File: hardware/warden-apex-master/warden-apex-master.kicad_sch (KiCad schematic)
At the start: 82 parts, among them IC1 SIM7080G, IC2 BQ24650RVAR, IC3 TPS63070RNMR, IC4 MAX98357AETE+T, J1 U.FL-R-SMT-1, J2 U.FL-R-SMT-1, J3 61300211121, J4 Expansion_Header, J5 Qwiic, Q1 DMG9926UDM, Q2 AO3401A, Q3 2N7002, U1 113991115, U2 Ai-Thinker-Ra-01, U3 M138 Modem, U4 MCP23017_SO, U5 SRV05-4-P-T7, U6 SC16IS740, X1 14.7456MHz

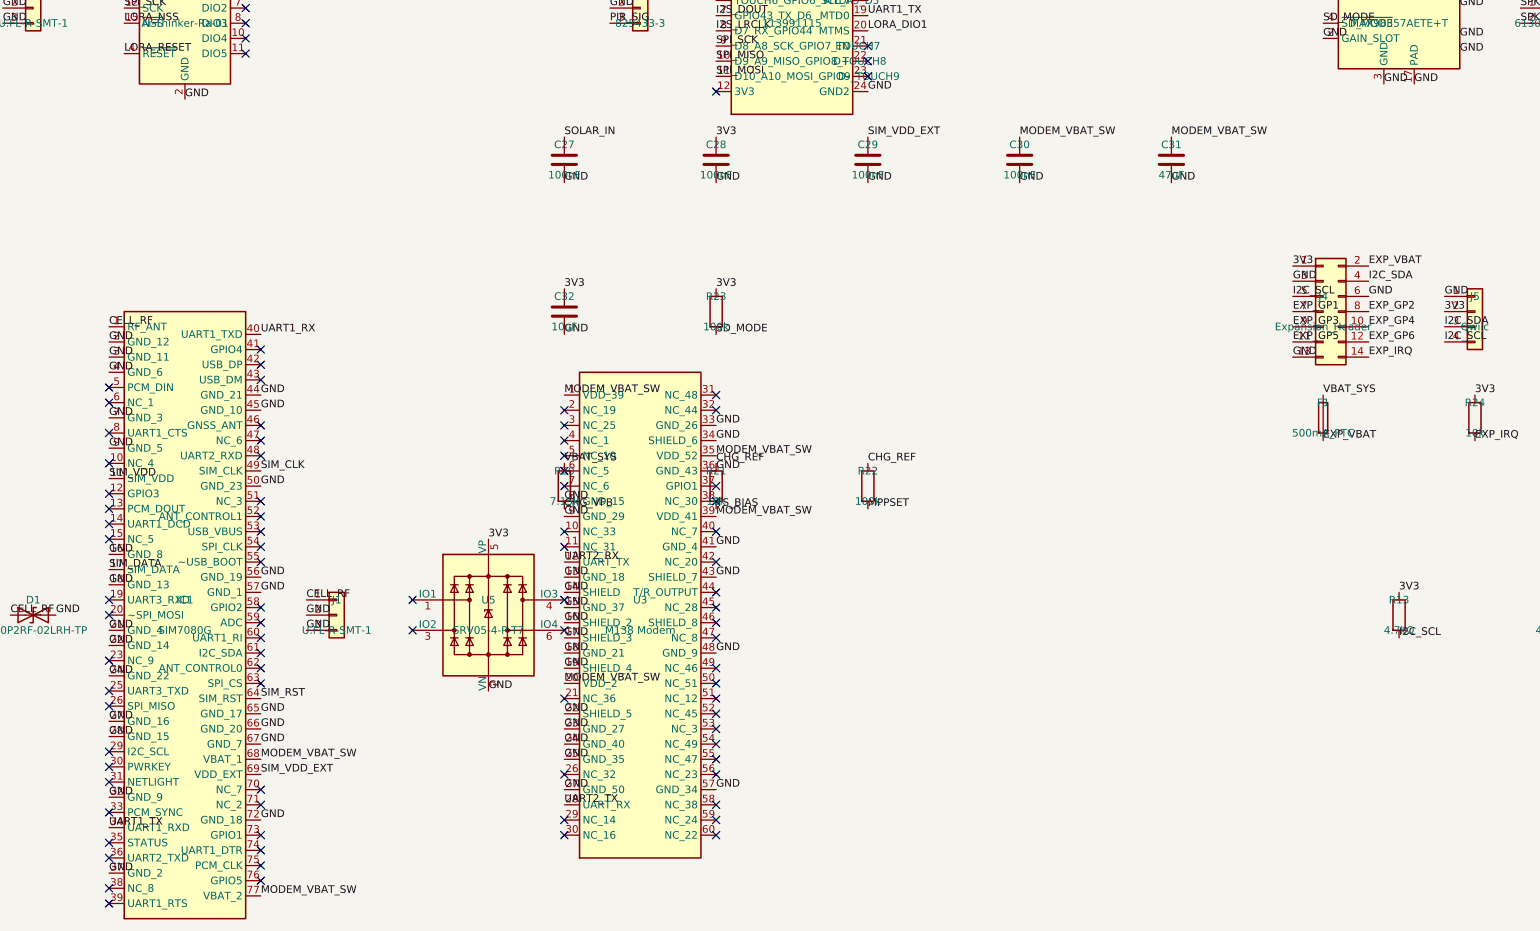
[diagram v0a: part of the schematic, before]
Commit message: Update warden-apex design for Phase 21 SIM7080 repair. Adjusted BOM files to include new capacitor C33 and updated component placements for C34. Revised Gerber files with new timestamps and corrected net connections for UART signals. Enhanced README.md with details on the repair process and updated upload instructions for JLCPCB.
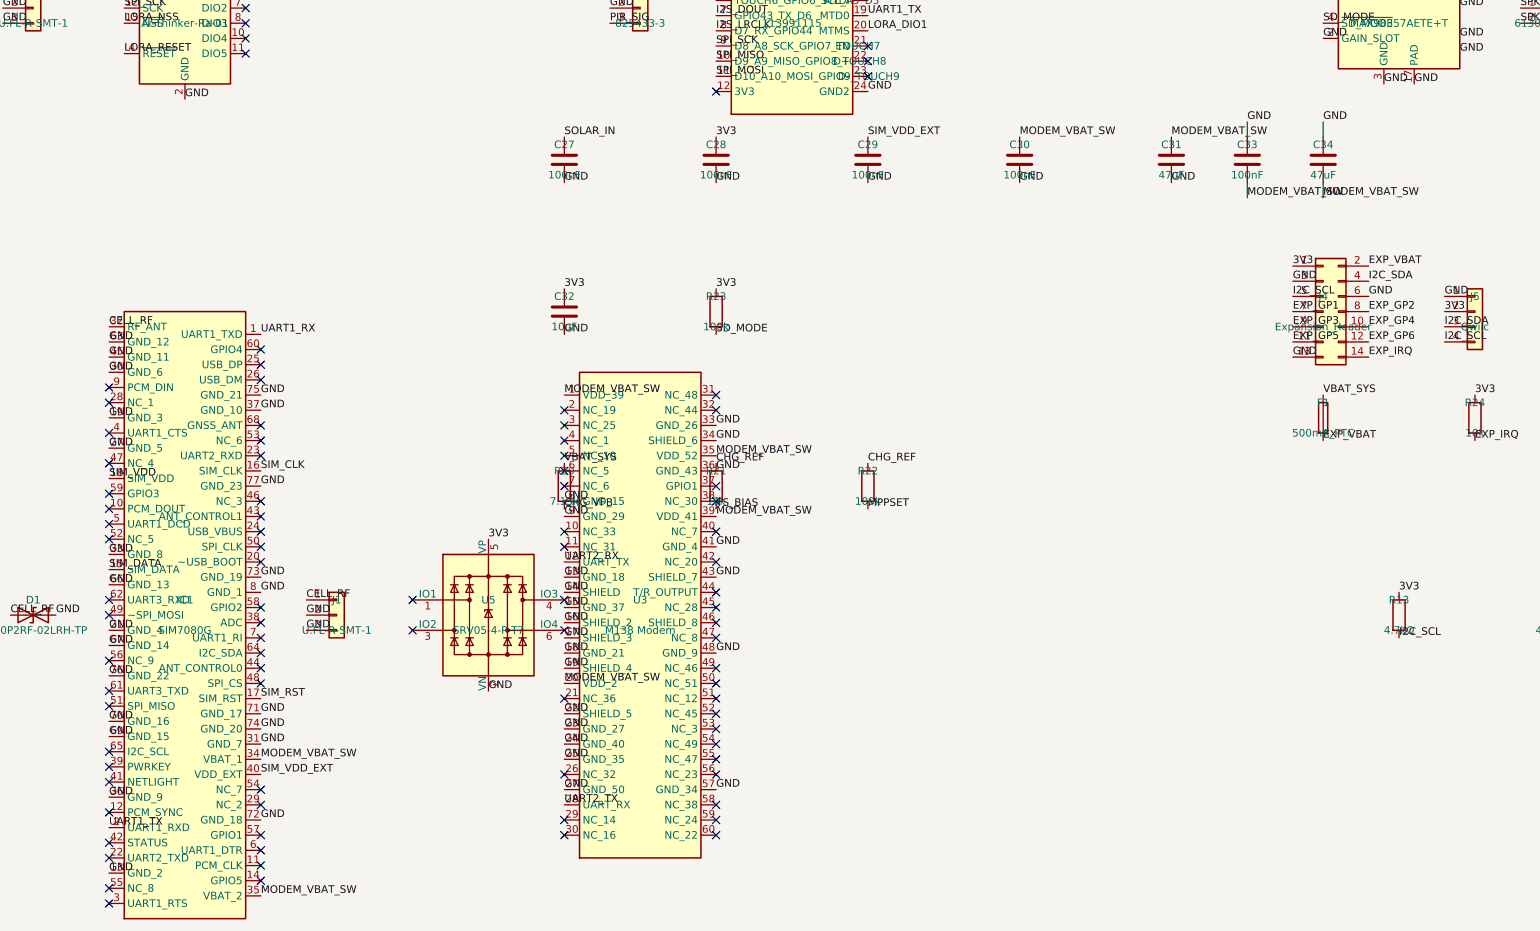
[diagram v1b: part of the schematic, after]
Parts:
- added C33: 100nF, Capacitor_SMD:C_0805_2012Metric, symbol Device:C
- added C34: 47uF, Capacitor_SMD:C_1206_3216Metric, symbol Device:C
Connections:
- net CELL_RF: now also IC1.32 (RF_ANT); no longer IC1.1 (RF_ANT)
- net GND: now also IC1.13 (GND_2), IC1.19 (GND_3), IC1.30 (GND_6), IC1.31 (GND_7), IC1.33 (GND_8), IC1.36 (GND_9), IC1.63 (GND_12), IC1.69 (GND_15), IC1.70 (GND_16), IC1.71 (GND_17), IC1.73 (GND_19), IC1.74 (GND_20), IC1.75 (GND_21), IC1.76 (GND_22), IC1.77 (GND_23), IC1.8 (GND_1), C33.1, C34.1; no longer IC1.16 (GND_8), IC1.18 (GND_13), IC1.2 (GND_12), IC1.22 (GND_14), IC1.24 (GND_22), IC1.28 (GND_15), IC1.3 (GND_11), IC1.32 (GND_9), IC1.4 (GND_6), IC1.44 (GND_21), IC1.50 (GND_23), IC1.56 (GND_19), IC1.57 (GND_1), IC1.65 (GND_17), IC1.7 (GND_3), IC1.9 (GND_5)
- net MODEM_VBAT_SW: now also IC1.34 (VBAT_1), IC1.35 (VBAT_2), C33.2, C34.2; no longer IC1.68 (VBAT_1), IC1.77 (VBAT_2)
- net SIM_CLK: now also IC1.16 (SIM_CLK); no longer IC1.49 (SIM_CLK)
- net SIM_DATA: now also IC1.15 (SIM_DATA); no longer IC1.17 (SIM_DATA)
- net SIM_RST: now also IC1.17 (SIM_RST); no longer IC1.64 (SIM_RST)
- net SIM_VDD: now also IC1.18 (SIM_VDD); no longer IC1.11 (SIM_VDD)
- net SIM_VDD_EXT: now also IC1.40 (VDD_EXT); no longer IC1.69 (VDD_EXT)
- net UART1_RX: now also IC1.1 (UART1_TXD); no longer IC1.40 (UART1_TXD)
- net UART1_TX: now also IC1.2 (UART1_RXD); no longer IC1.34 (UART1_RXD)

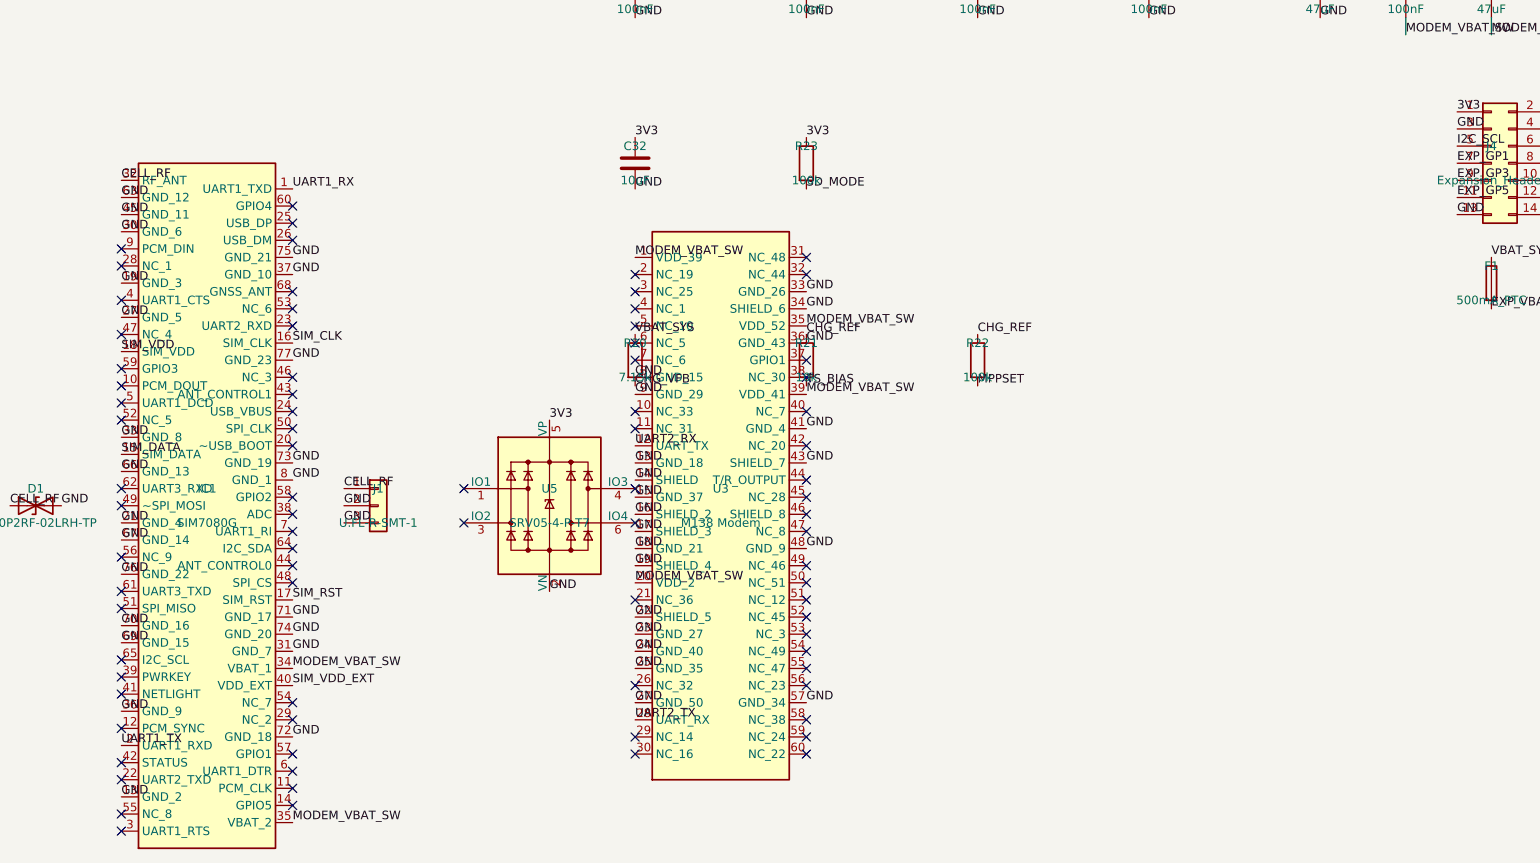
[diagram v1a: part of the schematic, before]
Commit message: Update warden-apex design with new components and routing improvements. Added capacitors C35 and C36, and resistor R25 to the BOM files. Adjusted Gerber files with updated timestamps and ensured UART1 routes through U7 with proper decoupling. Enhanced README.md with a summary of changes and upload readiness for JLCPCB.
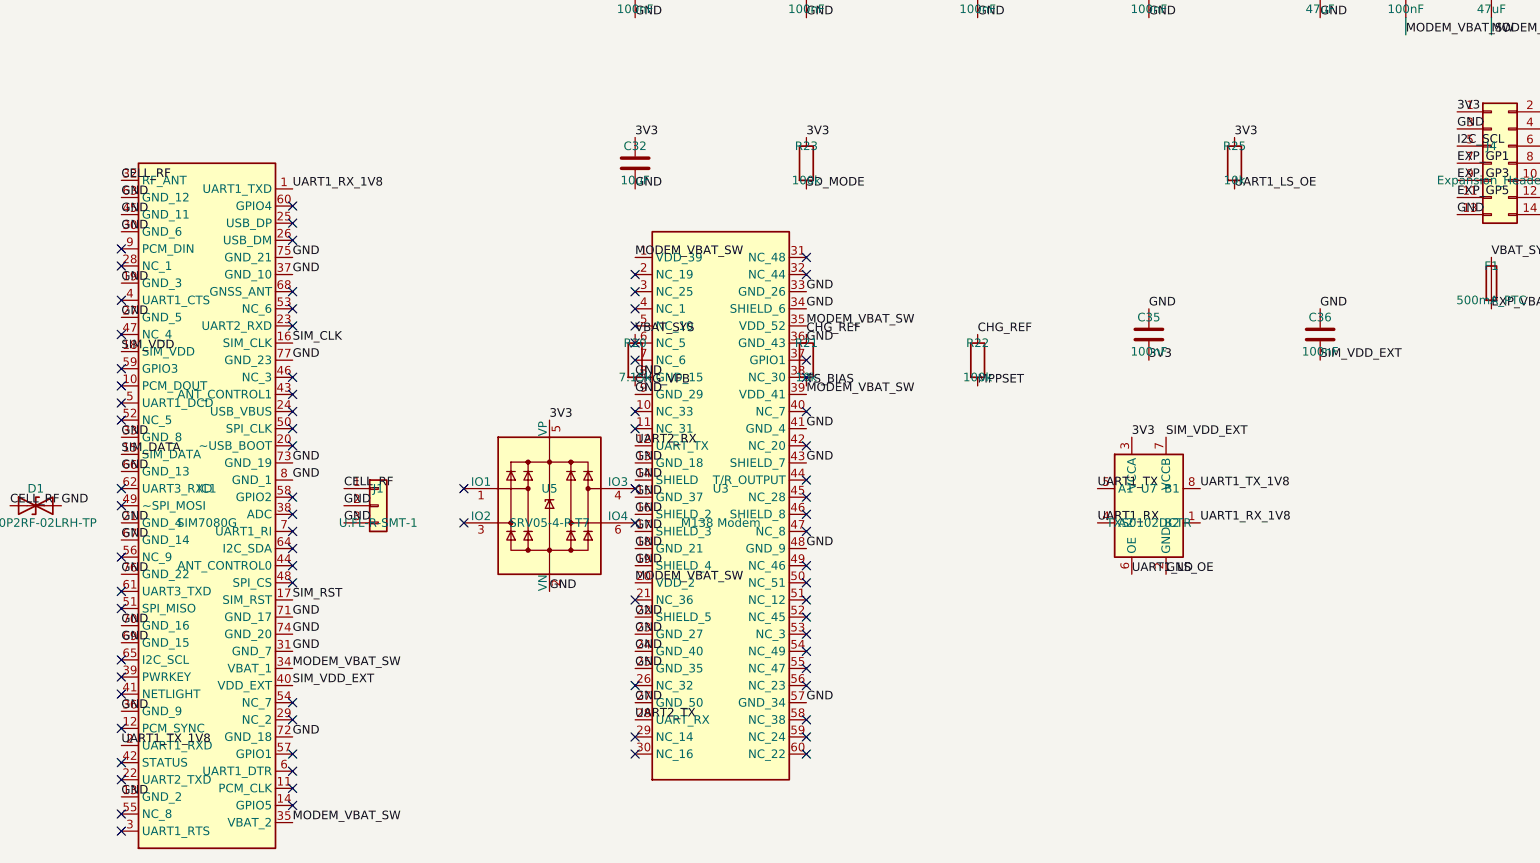
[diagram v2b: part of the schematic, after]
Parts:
- added C35, C36: 100nF, Capacitor_SMD:C_0402_1005Metric, symbol Device:C
- added R25: 10k, Resistor_SMD:R_0402_1005Metric, symbol Device:R
- added U7: TXS0102DCTR, Package_SO:TSSOP-8_3x3mm_P0.65mm, symbol warden_custom:TXS0102
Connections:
- net 3V3: now also C35.2, R25.1, U7.3 (VCCA)
- net GND: now also C35.1, C36.1, U7.2 (GND)
- net SIM_VDD_EXT: now also C36.2, U7.7 (VCCB)
- net UART1_RX: now also U7.4 (A2); no longer IC1.1 (UART1_TXD)
- net UART1_TX: now also U7.5 (A1); no longer IC1.2 (UART1_RXD)
- new net UART1_LS_OE: R25.2, U7.6 (OE)
- new net UART1_RX_1V8: IC1.1 (UART1_TXD), U7.1 (B2)
- new net UART1_TX_1V8: IC1.2 (UART1_RXD), U7.8 (B1)

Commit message: Refine warden-apex design by removing unused components C35, C36, and R25 from BOM files. Update README.md to reflect UART1 routing changes, now directly connecting between U1 and IC1. Revise Gerber files with new timestamps and ensure consistency across documentation. Clean up schematic with follow-on parity adjustments, resulting in zero schematic-parity warnings.
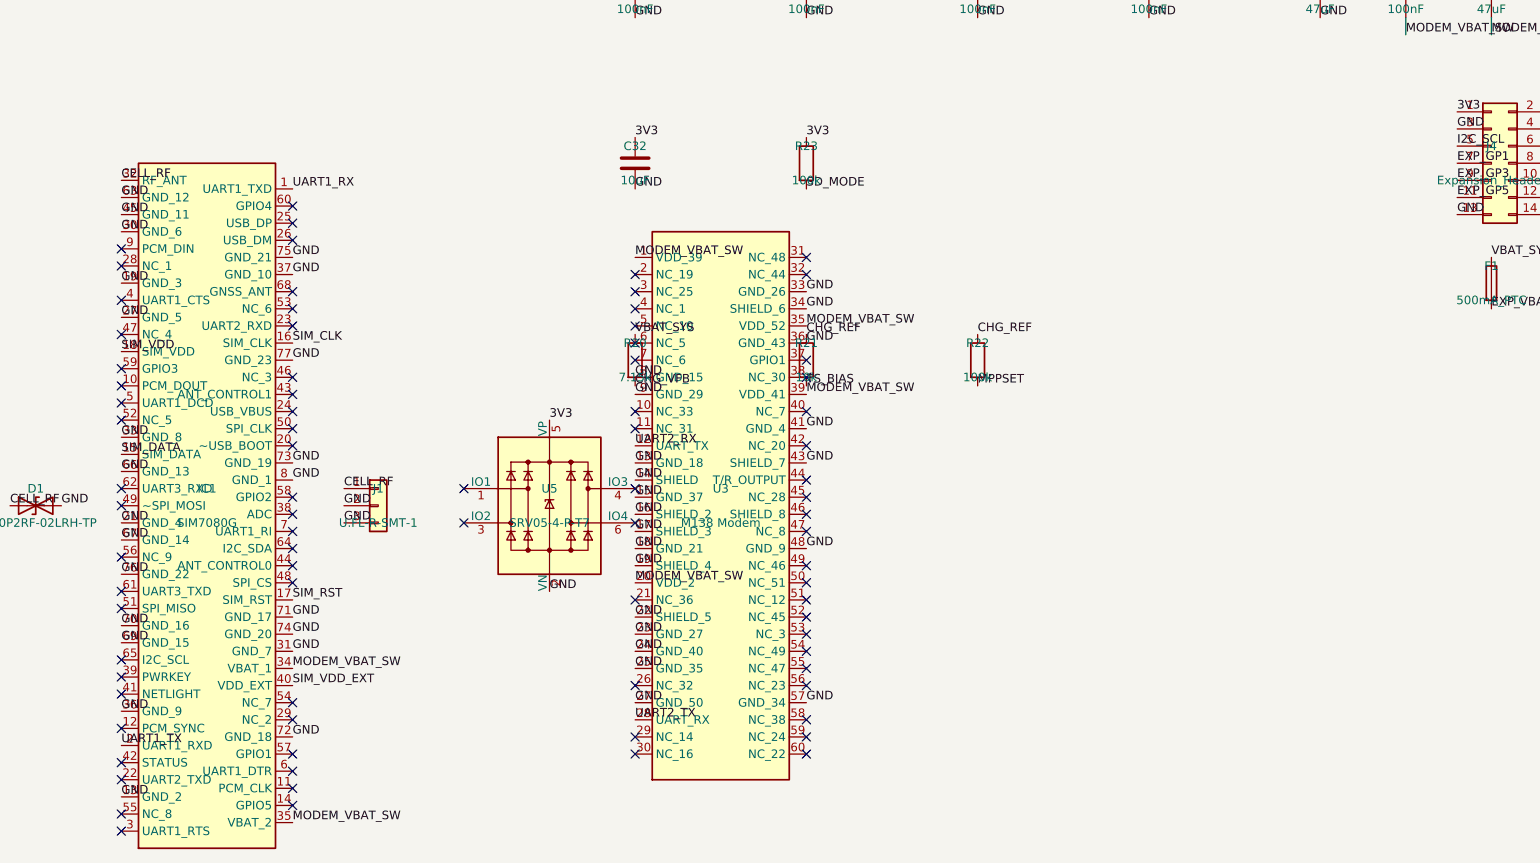
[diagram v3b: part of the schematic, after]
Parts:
- removed C35, C36: 100nF, Capacitor_SMD:C_0402_1005Metric, symbol Device:C
- removed R25: 10k, Resistor_SMD:R_0402_1005Metric, symbol Device:R
- removed U7: TXS0102DCTR, Package_SO:TSSOP-8_3x3mm_P0.65mm, symbol warden_custom:TXS0102
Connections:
- net UART1_RX_1V8 is gone; now on net UART1_RX: IC1.1 (UART1_TXD)
- net UART1_TX_1V8 is gone; now on net UART1_TX: IC1.2 (UART1_RXD)
